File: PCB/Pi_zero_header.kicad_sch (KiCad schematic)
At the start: 37 parts, among them J1 Raspberry_Pi_2_3, J2 USB_C_Receptacle_USB2.0, U1 RP2040, U2 W25Q128JVS, U3 TB6612FNG, U4 NCP1117-3.3_SOT223, Y1 Crystal

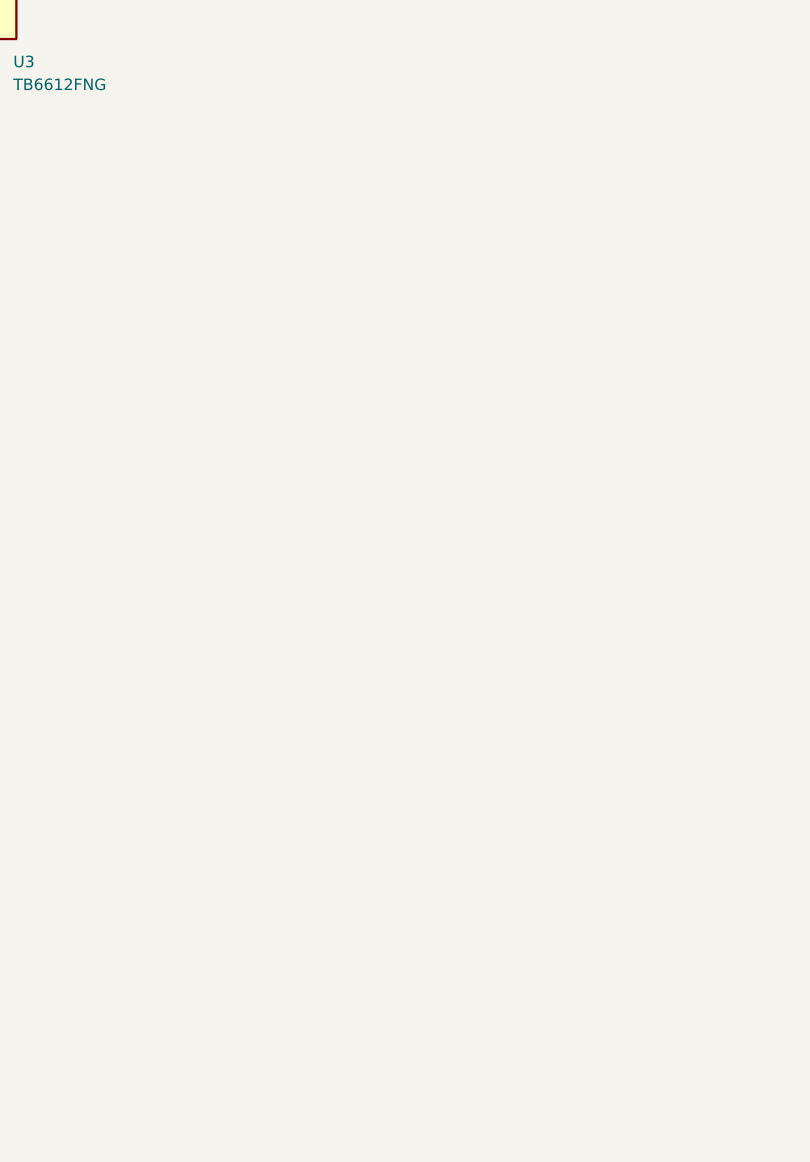
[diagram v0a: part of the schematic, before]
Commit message: Updated and added TI charger
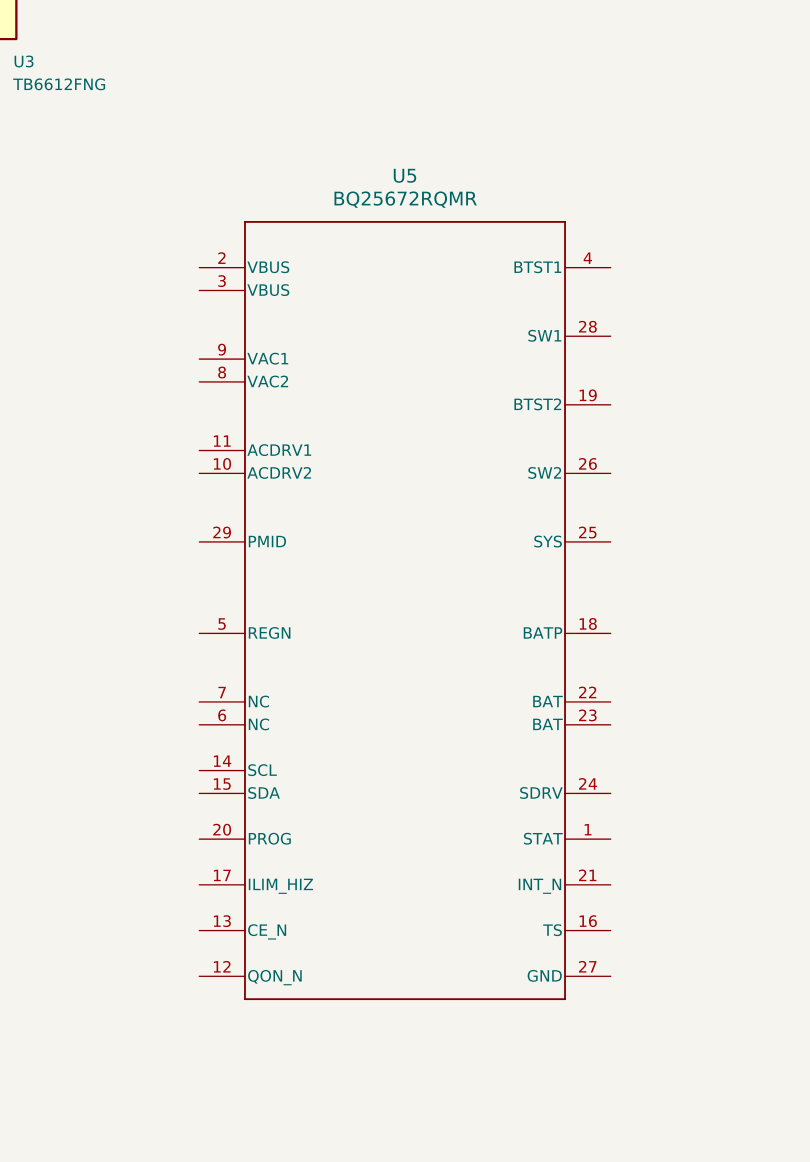
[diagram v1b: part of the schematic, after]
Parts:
- added U5: BQ25672RQMR, RQM0029A-MFG:RQM0029A-MFG, symbol BQ25672RQMR:BQ25672RQMR
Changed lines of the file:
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@@
+    )
+  )
+  (symbol (lib_id "BQ25672RQMR:BQ25672RQMR") (at 313.69 151.13 0) (unit 1)
+    (in_bom yes) (on_board yes) (dnp no) (fields_autoplaced)
+    (property "Reference" "U5" (at 336.55 140.97 0)
+      (effects (font (size 1.524 1.524)))
+    )
+    (property "Value" "BQ25672RQMR" (at 336.55 143.51 0)
+      (effects (font (size 1.524 1.524)))
+    )
+    (property "Footprint" "RQM0029A-MFG:RQM0029A-MFG" (at 313.69 151.13 0)
+      (effects (font (size 1.27 1.27) italic) hide)
+    )
+    (property "Datasheet" "BQ25672RQMR" (at 313.69 151.13 0)
+      (effects (font (size 1.27 1.27) italic) hide)
+    )
+    (pin "20")
+    (pin "5")
+    (pin "2")
+    (pin "6")
+    (pin "25")
+    (pin "19")
+    (pin "28")
+    (pin "10")
+    (pin "13")
+    (pin "17")
+    (pin "9")
+    (pin "24")
+    (pin "8")
+    (pin "27")
+    (pin "15")
+    (pin "16")
+    (pin "21")
+    (pin "7")
+    (pin "14")
+    (pin "22")
+    (pin "1")
+    (pin "12")
+    (pin "26")
+    (pin "3")
+    (pin "4")
+    (pin "23")
+    (pin "11")
+    (pin "29")
+    (pin "18")
+    (instances
+      (project "Pi_zero_header"
+        (path "/b619a5d9-7fc7-4364-bf63-192bb5e8977a"
+          (reference "U5") (unit 1)
+        )
+      )
     )
   )

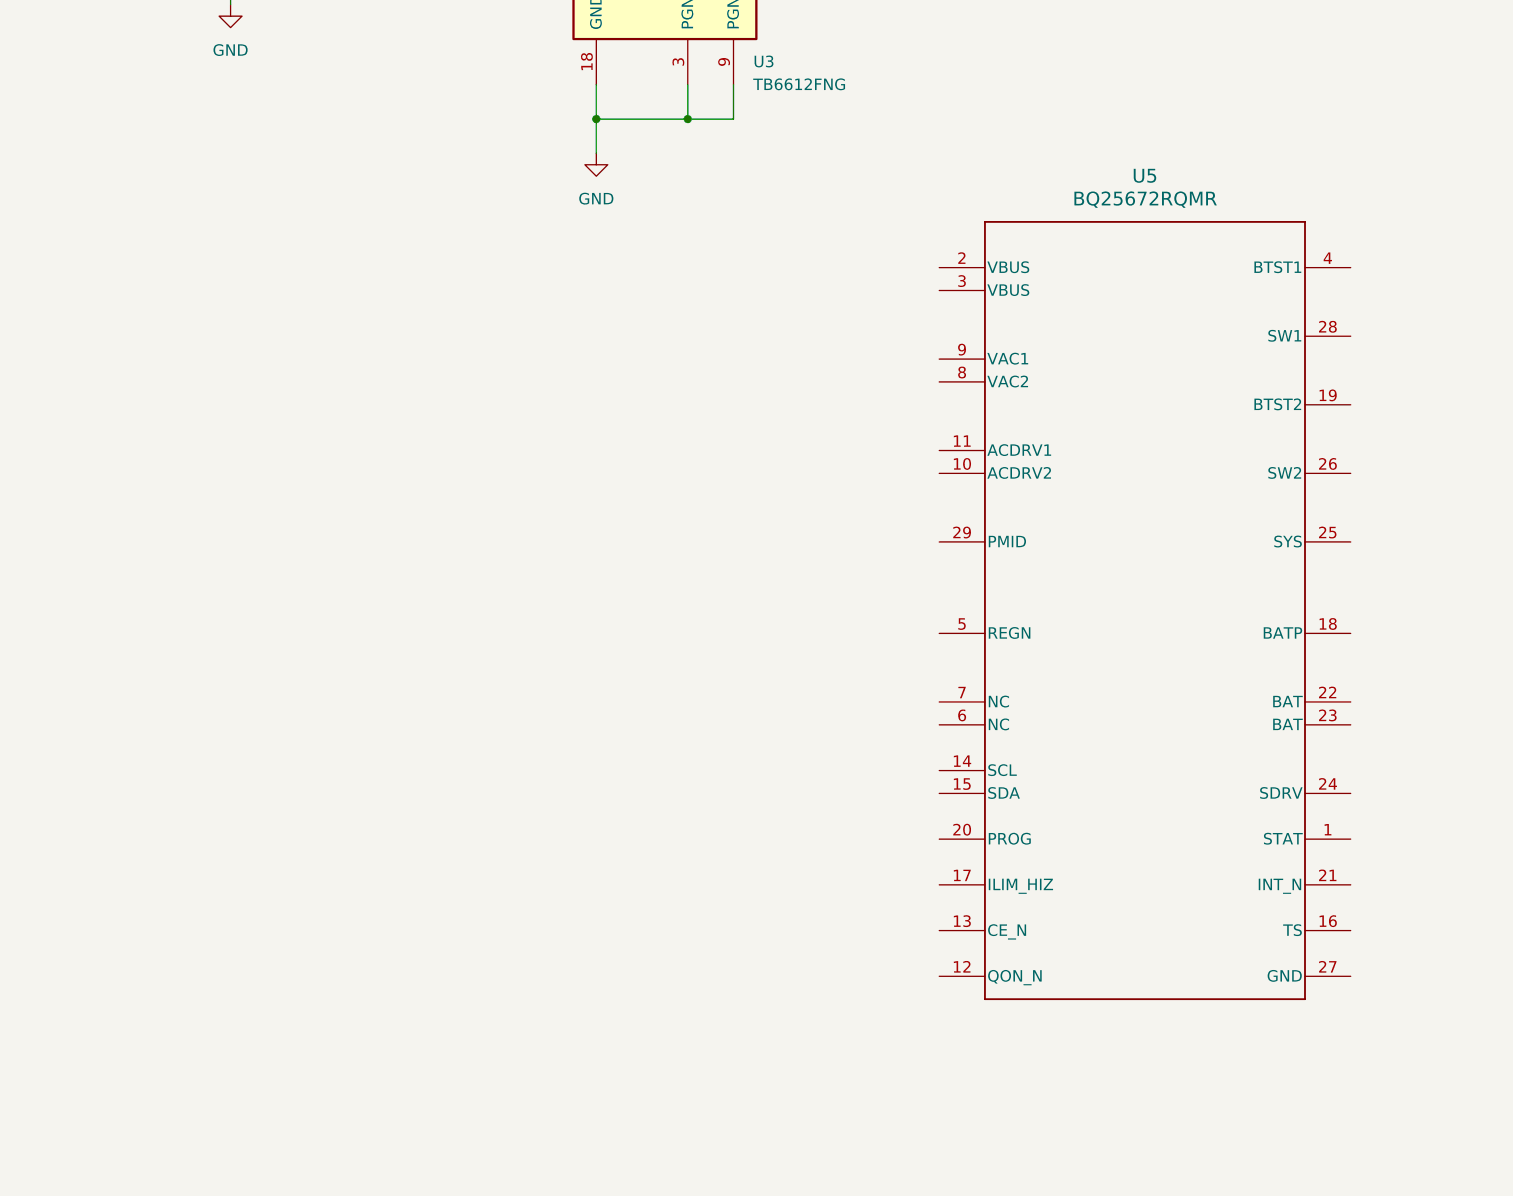
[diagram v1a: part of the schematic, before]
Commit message: Moved added parts to corretc folders
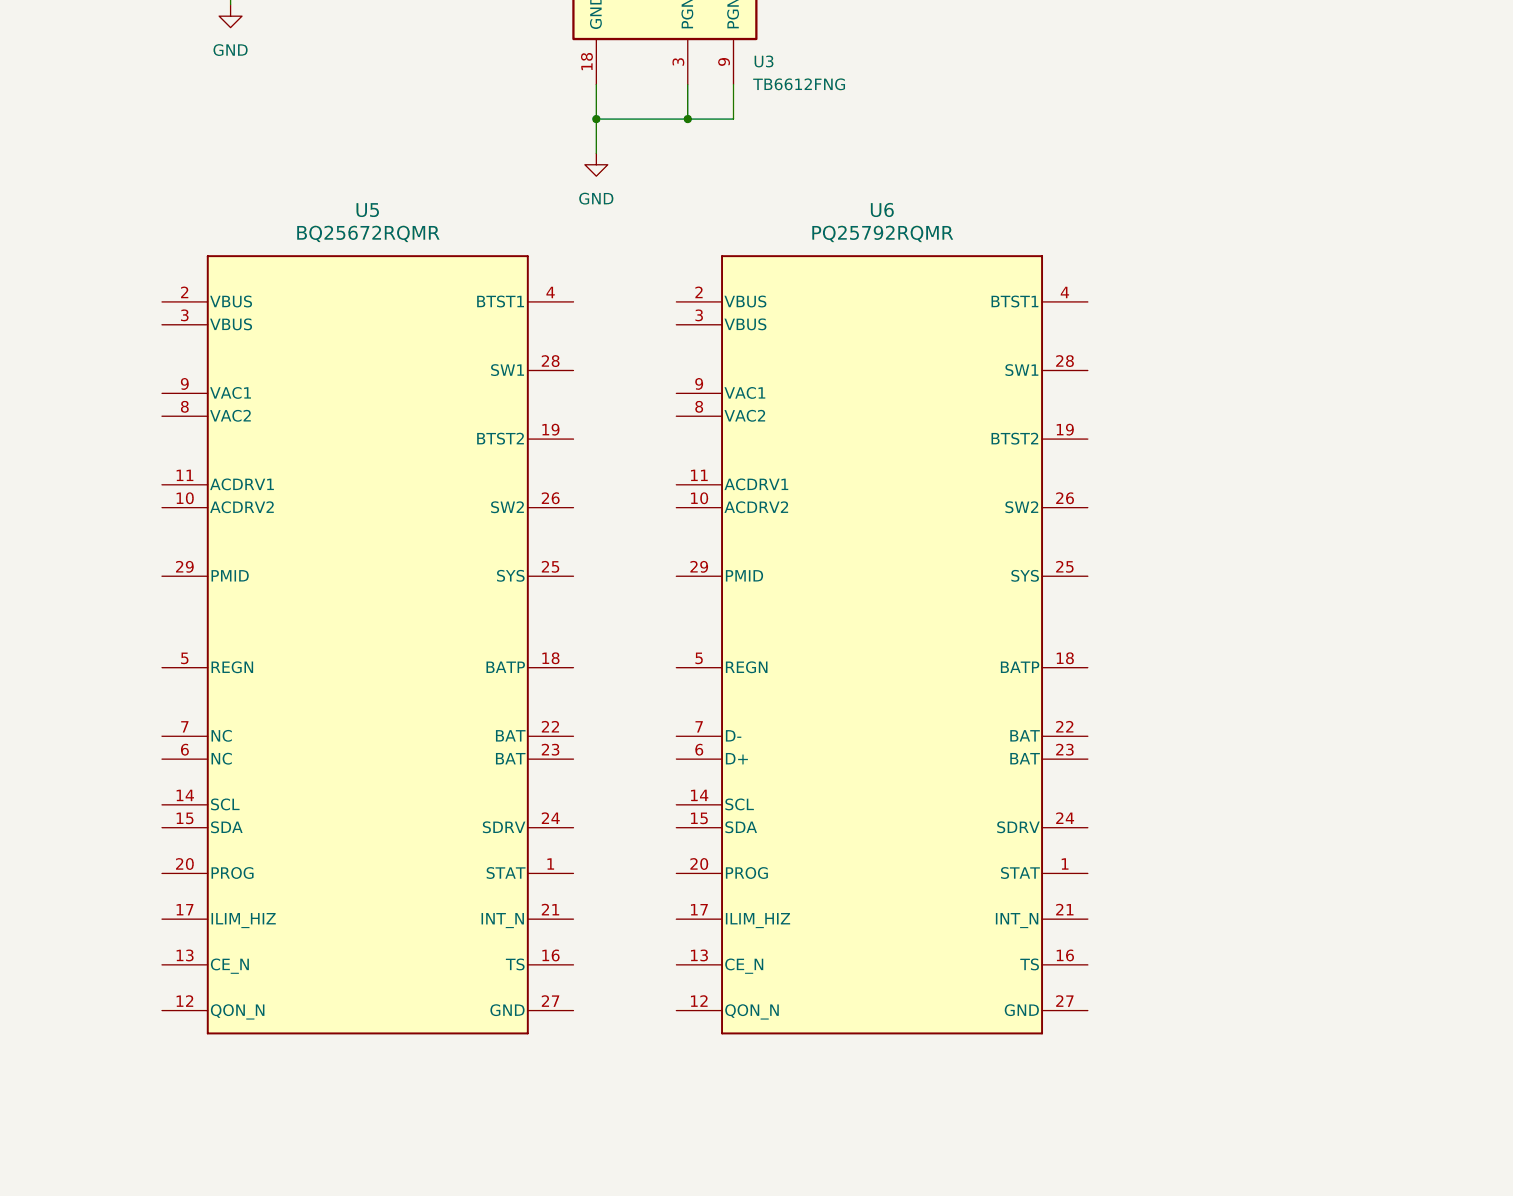
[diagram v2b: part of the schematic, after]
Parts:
- added U6: PQ25792RQMR, RQM0029A-MFG:RQM0029A-MFG, symbol BQ25792RQMR:PQ25792RQMR
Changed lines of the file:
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@@
+    )
+  )
+  (symbol (lib_id "BQ25672RQMR:BQ25672RQMR") (at 227.33 154.94 0) (unit 1)
+    (in_bom yes) (on_board yes) (dnp no) (fields_autoplaced)
+    (property "Reference" "U5" (at 250.19 144.78 0)
+      (effects (font (size 1.524 1.524)))
+    )
+    (property "Value" "BQ25672RQMR" (at 250.19 147.32 0)
+      (effects (font (size 1.524 1.524)))
+    )
+    (property "Footprint" "RQM0029A-MFG:RQM0029A-MFG" (at 227.33 154.94 0)
+      (effects (font (size 1.27 1.27) italic) hide)
+    )
+    (property "Datasheet" "BQ25672RQMR" (at 227.33 154.94 0)
+      (effects (font (size 1.27 1.27) italic) hide)
+    )
+    (pin "29")
+    (pin "28")
+    (pin "18")
+    (pin "26")
+    (pin "27")
+    (pin "5")
+    (pin "24")
+    (pin "25")
+    (pin "9")
+    (pin "15")
+    (pin "22")
+    (pin "23")
+    (pin "4")
+    (pin "21")
+    (pin "10")
+    (pin "12")
+    (pin "19")
+    (pin "13")
+    (pin "7")
+    (pin "1")
+    (pin "20")
+    (pin "3")
+    (pin "6")
+    (pin "8")
+    (pin "16")
+    (pin "14")
+    (pin "11")
+    (pin "17")
+    (pin "2")
+    (instances
+      (project "Pi_zero_header"
+        (path "/b619a5d9-7fc7-4364-bf63-192bb5e8977a"
+          (reference "U5") (unit 1)
+        )
+      )
     )
   )
@@
     )
   )
+  (symbol (lib_id "BQ25792RQMR:PQ25792RQMR") (at 284.48 154.94 0) (unit 1)
+    (in_bom yes) (on_board yes) (dnp no) (fields_autoplaced)
+    (property "Reference" "U6" (at 307.34 144.78 0)
+      (effects (font (size 1.524 1.524)))
+    )
+    (property "Value" "PQ25792RQMR" (at 307.34 147.32 0)
+      (effects (font (size 1.524 1.524)))
+    )
+    (property "Footprint" "RQM0029A-MFG:RQM0029A-MFG" (at 284.48 154.94 0)
+      (effects (font (size 1.27 1.27) italic) hide)
+    )
+    (property "Datasheet" "PQ25792RQMR" (at 284.48 154.94 0)
+      (effects (font (size 1.27 1.27) italic) hide)
+    )
+    (pin "9")
+    (pin "24")
+    (pin "20")
+    (pin "12")
+    (pin "23")
+    (pin "14")
+    (pin "7")
+    (pin "29")
+    (pin "4")
+    (pin "19")
+    (pin "3")
+    (pin "16")
+    (pin "28")
+    (pin "13")
+    (pin "11")
+    (pin "17")
+    (pin "21")
+    (pin "26")
+    (pin "10")
+    (pin "27")
+    (pin "22")
+    (pin "5")
+    (pin "25")
+    (pin "1")
+    (pin "18")
+    (pin "6")
+    (pin "15")
+    (pin "8")
+    (pin "2")
+    (instances
+      (project "Pi_zero_header"
+        (path "/b619a5d9-7fc7-4364-bf63-192bb5e8977a"
+          (reference "U6") (unit 1)
+        )
+      )
+    )
+  )
   (symbol (lib_id "power:GND") (at 182.88 162.56 0) (unit 1)
     (in_bom yes) (on_board yes) (dnp no) (fields_autoplaced)
@@
         )
       )
-    )
-  )
-  (symbol (lib_id "BQ25672RQMR:BQ25672RQMR") (at 313.69 151.13 0) (unit 1)
-    (in_bom yes) (on_board yes) (dnp no) (fields_autoplaced)
-    (property "Reference" "U5" (at 336.55 140.97 0)
-      (effects (font (size 1.524 1.524)))
-    )
-    (property "Value" "BQ25672RQMR" (at 336.55 143.51 0)
-      (effects (font (size 1.524 1.524)))
-    )
-    (property "Footprint" "RQM0029A-MFG:RQM0029A-MFG" (at 313.69 151.13 0)
-      (effects (font (size 1.27 1.27) italic) hide)
-    )
-    (property "Datasheet" "BQ25672RQMR" (at 313.69 151.13 0)
-      (effects (font (size 1.27 1.27) italic) hide)
-    )
-    (pin "20")
-    (pin "5")
-    (pin "2")
-    (pin "6")
-    (pin "25")
-    (pin "19")
-    (pin "28")
-    (pin "10")
-    (pin "13")
-    (pin "17")
-    (pin "9")
-    (pin "24")
-    (pin "8")
-    (pin "27")
-    (pin "15")
-    (pin "16")
-    (pin "21")
-    (pin "7")
-    (pin "14")
-    (pin "22")
-    (pin "1")
-    (pin "12")
-    (pin "26")
-    (pin "3")
-    (pin "4")
-    (pin "23")
-    (pin "11")
-    (pin "29")
-    (pin "18")
-    (instances
-      (project "Pi_zero_header"
-        (path "/b619a5d9-7fc7-4364-bf63-192bb5e8977a"
-          (reference "U5") (unit 1)
-        )
-      )

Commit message: Changed PCB design
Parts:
- removed U4: NCP1117-3.3_SOT223, Package_TO_SOT_SMD:SOT-223-3_TabPin2, symbol Regulator_Linear:NCP1117-3.3_SOT223
- removed U5: BQ25672RQMR, RQM0029A-MFG:RQM0029A-MFG, symbol BQ25672RQMR:BQ25672RQMR
- added C22, C23, C26: 0.1u, symbol Device:C
- added C24, C25, C27, C28: 10u, symbol Device:C
- H1, H2, H3, H4: footprint (none) -> MountingHole:MountingHole_2.7mm_M2.5
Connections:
- net +3V3: no longer J1.1 (3V3), J1.17 (3V3)
- net +5V: now also J1.2 (5V), J1.4 (5V)
- net GND: now also U6.10 (ACDRV2), U6.11 (ACDRV1), U6.27 (GND), C22.2, C23.2, C24.2, C25.2, C26.2, C27.2, C28.2
- net USB_D+: now also U6.6 (D+)
- net USB_D-: now also U6.7 (D-)
- net VBUS: now also U6.2 (VBUS), U6.3 (VBUS), C22.1, C23.1, C24.1, C25.1; no longer J1.2 (5V), J1.4 (5V)
- net SCL_PWR: now reaches U6.14 (SCL)
- net SDA_PWR: now reaches U6.15 (SDA)
- net at U6.22 (BAT): now also U6.23 (BAT)
- net at U6.29 (PMID): now also C26.1, C27.1, C28.1
- net at U6.8 (VAC2): now also U6.9 (VAC1)
